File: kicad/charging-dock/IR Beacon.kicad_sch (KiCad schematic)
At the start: 10 parts, among them Q8 IRLML6344TRPBF, U3 TLC555CDR

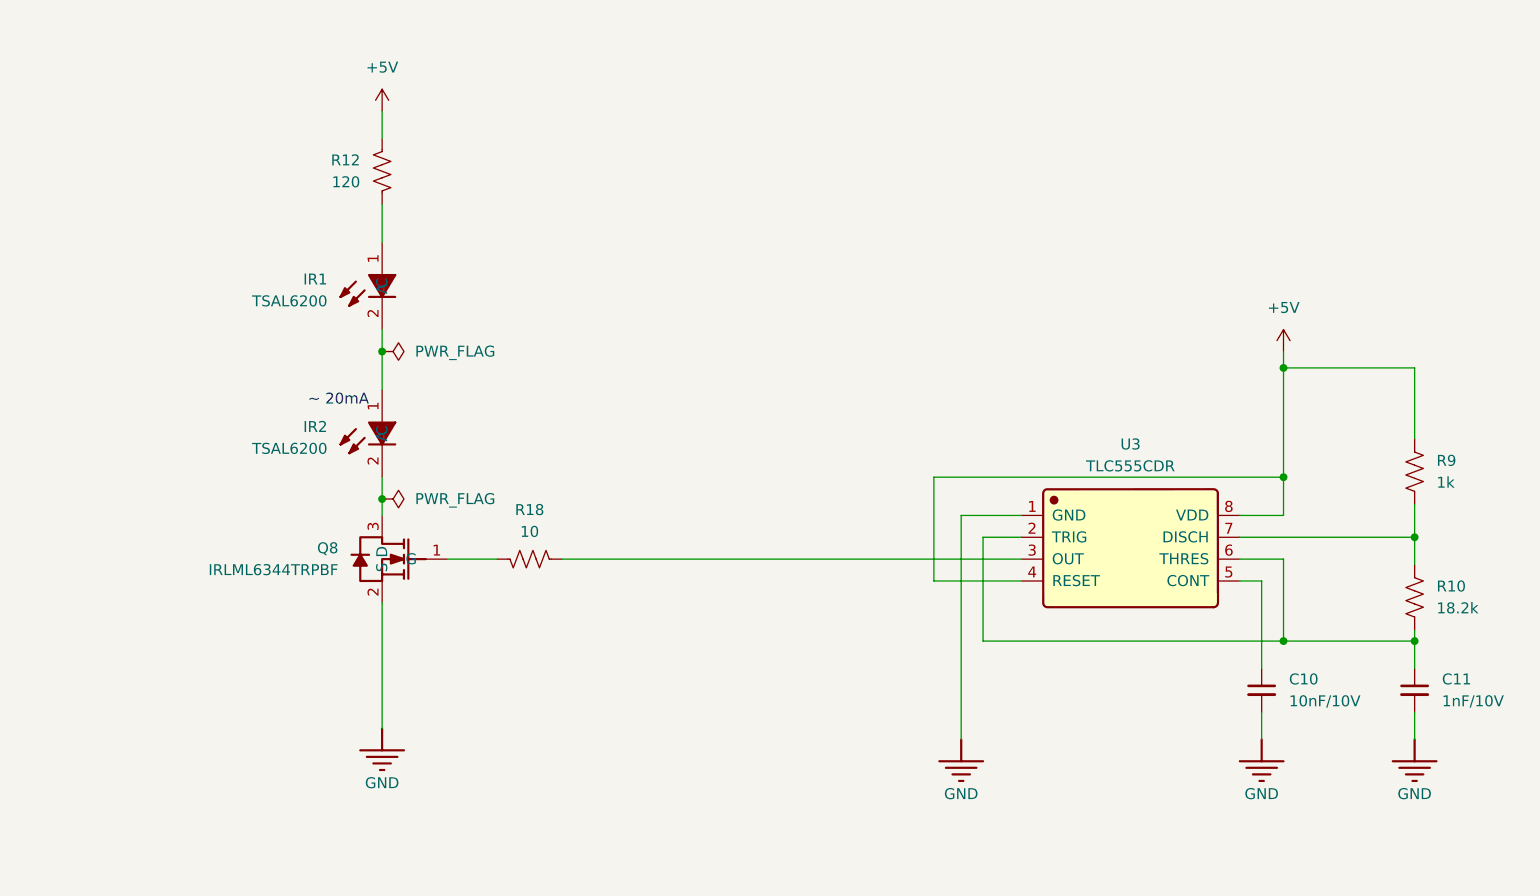
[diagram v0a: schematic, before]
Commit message: Charging dock rev 2; main-phone bucks AP64501 -> TPS54560B
Charging dock (kicad/charging-dock), redesigned:
- CH32V003F4P6 control (Arduino core, ch32fun, PlatformIO)
- robot detection: resistance-signature probe before DOCK+ goes live
- AO4407C soft-start output switch, 50 mOhm + INA180A1 current sense
- NEC IR beacon: two 3x TSAL6200 strings, AC-coupled gates
- 20 V input: DC-044A-20A, 5 A fuse, SMAJ22A, HT7533-1
- refs 8xxx for the one-panel plan; uses the shared ../main libraries
- removed the orphan sheets, the old local library copy and an unrelated PDF
- README with pin map, detection math, firmware rules, layout notes

main-phone: U21/U22 TPS54560B (AP64501 out of stock) with SS56 catch
diodes, 232k RT, 4.7k + 47nF compensation, U21 EN divider; BAT-VCC input
caps 10uF/50V 1206. SPEC and READMEs updated.

Co-Authored-By: Claude Opus 5.5 (1M context) <noreply@anthropic.com>
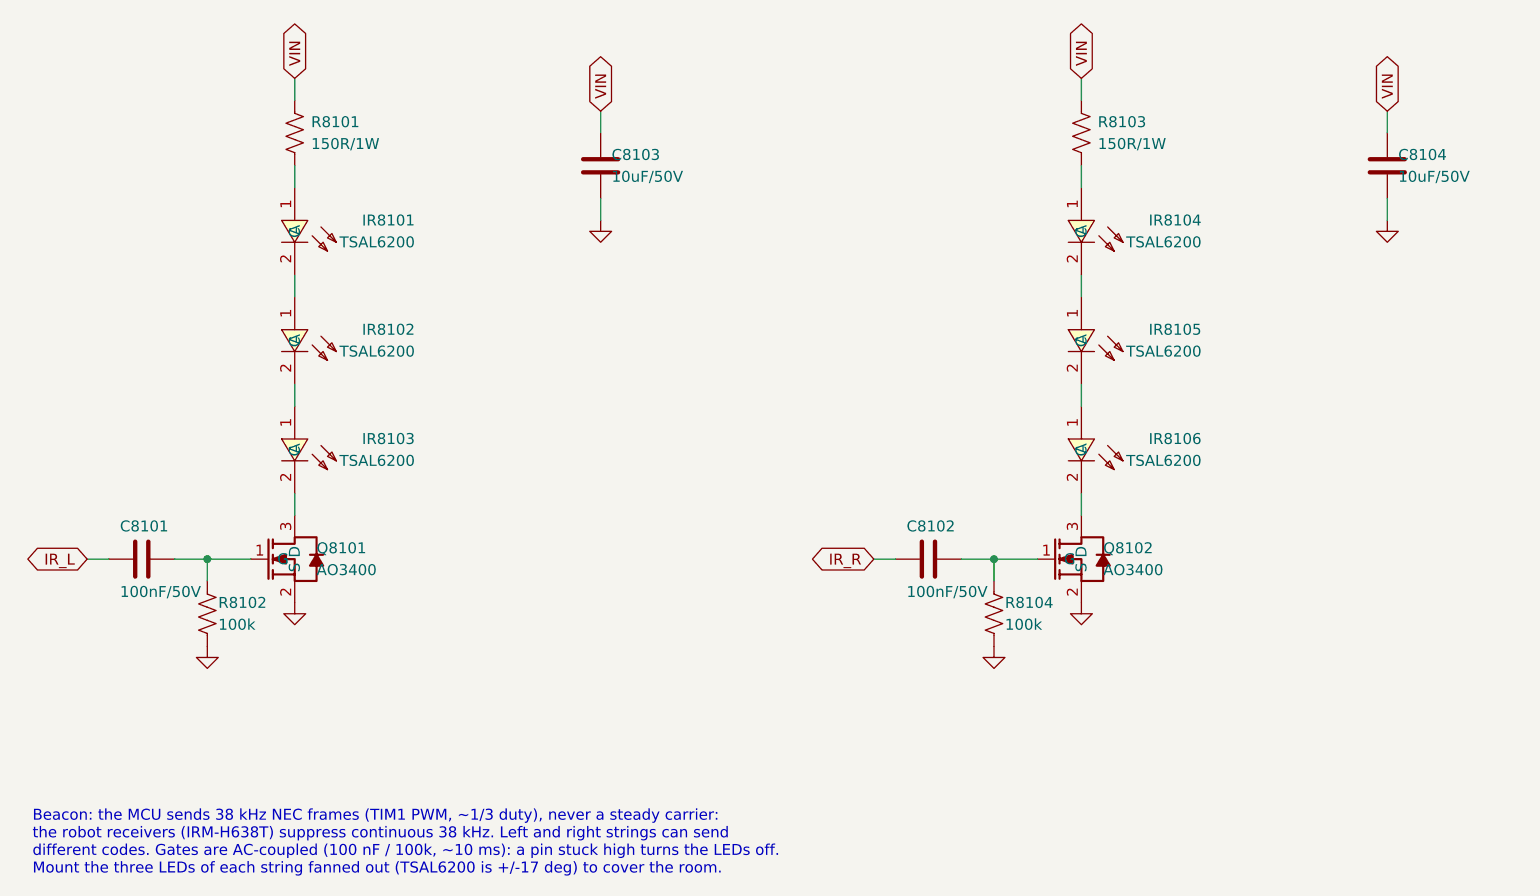
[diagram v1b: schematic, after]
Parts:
- removed C10: 10nF/10V, symbol Device:C_Small
- removed C11: 1nF/10V, symbol Device:C_Small
- removed IR1, IR2: TSAL6200, JLCImport:TSAL6200, symbol JLCImport:TSAL6200
- removed Q8: IRLML6344TRPBF, JLCImport:IRLML6344TRPBF, symbol JLCImport:IRLML6344TRPBF
- removed R10: 18.2k, symbol Device:R_US
- removed R12: 120, symbol Device:R_US
- removed R18: 10, symbol Device:R_US
- removed R9: 1k, symbol Device:R_US
- removed U3: TLC555CDR, JLCImport:TLC555CDR, symbol JLCImport:TLC555CDR
- added C8101, C8102: 100nF/50V, Capacitor_SMD:C_0603_1608Metric, symbol Device:C
- added C8103, C8104: 10uF/50V, Capacitor_SMD:C_1206_3216Metric, symbol Device:C
- added IR8101, IR8102, IR8103, IR8104, IR8105, IR8106: TSAL6200, JLCImport:TSAL6200, symbol JLCImport:TSAL6200
- added Q8101, Q8102: AO3400, JLCImport:AO3400, symbol JLCImport:AO3400
- added R8101, R8103: 150R/1W, Resistor_SMD:R_2512_6332Metric, symbol Device:R_US
- added R8102, R8104: 100k, Resistor_SMD:R_0603_1608Metric, symbol Device:R_US
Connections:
- net GND: now also C8103.2, C8104.2, Q8101.2 (S), Q8102.2 (S), R8102.2, R8104.2
- new net: C8102.2, Q8102.1 (G), R8104.1
- new net: IR8104.1 (A), R8103.2
- new net: IR8104.2 (C), IR8105.1 (A)
- new net: C8101.2, Q8101.1 (G), R8102.1
- new net: IR8101.1 (A), R8101.2
- new net: IR8103.2 (C), Q8101.3 (D)
- new net: IR8101.2 (C), IR8102.1 (A)
- new net: IR8102.2 (C), IR8103.1 (A)
- new net: IR8105.2 (C), IR8106.1 (A)
- new net: IR8106.2 (C), Q8102.3 (D)
- new net IR_L: C8101.1
- new net IR_R: C8102.1
- new net VIN: C8103.1, C8104.1, R8101.1, R8103.1
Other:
- note added: "Beacon: the MCU sends 38 kHz NEC frames (TIM1 PWM, ~1/3 duty), never a steady carrier: the robot receivers (IRM-H638T) suppress continuous 38 kHz. Left and right strings can send different codes. Gates are AC-coupled (100 nF / 100k, ~10 ms): a pin stuck high turns the LEDs off. Mount the three LEDs of each string fanned out (TSAL6200 is +/-17 deg) to cover the room."
- note removed: "~ 20mA"
- company: (none) -> OOMWOO charging dock
- title: (none) -> IR beacon

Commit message: Per-board reference ranges, J1 spare header, IMU AD0 pull-down, BOM outputs
- reference ranges: main-phone 1-999, dock 1000s, front ToF 2000s, side 3000s,
  cliff 4000s, rear IR 5000s, Hall 6000s (main-phone 7xxx parts renumbered
  below 1000; sensor boards and dock moved from 8xxx)
- main-phone: J7301 -> J1, a fitted 2x7 0.1" header with spares only
  (3.3 V, 5 V, I2C4, UART PC10/PC11, PA8-PA10, PD4, PE2, PE6, GND)
- IMU: AP_AD0 pulled low by R217 (address 0x68); INT2 on test pad TP1;
  FSYNC reachable on R211; R18/R72 removed
- tools/export.py replaces export_pdfs.py: schematic PDF and JLC-style BOM in
  each board's output/ folder; --pcb adds Gerbers, placement and STEP
- cliff and rear IR projects: fix top-level sheet left over from a copy
- Hall board: visual tidy-up

Co-Authored-By: Claude Opus 5.5 <noreply@anthropic.com>
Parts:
- renumbered C8101 to C1101, C8102 to C1102, C8103 to C1103, C8104 to C1104, IR8101 to IR1101, IR8102 to IR1102, IR8103 to IR1103, IR8104 to IR1104, IR8105 to IR1105, IR8106 to IR1106, Q8101 to Q1101, Q8102 to Q1102, R8101 to R1101, R8102 to R1102, R8103 to R1103, R8104 to R1104
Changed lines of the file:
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@@
 		(in_pos_files yes)
 		(dnp no)
-		(property "Reference" "R8101"
+		(property "Reference" "R1101"
 			(at 62.865 44.45 0)
 			(show_name no)
@@
 			(project "Charging Dock"
 				(path "/b1780c3e-7100-4df4-97c9-2fd6186fb125/4bb8f12b-f88e-462d-8d8b-7cab36a6773e"
-					(reference "R8101")
+					(reference "R1101")
 					(unit 1)
 				)
@@
 		(in_pos_files yes)
 		(dnp no)
-		(property "Reference" "IR8101"
+		(property "Reference" "IR1101"
 			(at 74.93 55.88 90)
 			(show_name no)
@@
 			(project "Charging Dock"
 				(path "/b1780c3e-7100-4df4-97c9-2fd6186fb125/4bb8f12b-f88e-462d-8d8b-7cab36a6773e"
-					(reference "IR8101")
+					(reference "IR1101")
 					(unit 1)
 				)
@@
 		(in_pos_files yes)
 		(dnp no)
-		(property "Reference" "IR8102"
+		(property "Reference" "IR1102"
 			(at 74.93 68.58 90)
 			(show_name no)
@@
 			(project "Charging Dock"
 				(path "/b1780c3e-7100-4df4-97c9-2fd6186fb125/4bb8f12b-f88e-462d-8d8b-7cab36a6773e"
-					(reference "IR8102")
+					(reference "IR1102")
 					(unit 1)
 				)
@@
 		(in_pos_files yes)
 		(dnp no)
-		(property "Reference" "IR8103"
+		(property "Reference" "IR1103"
 			(at 74.93 81.28 90)
 			(show_name no)
@@
 			(project "Charging Dock"
 				(path "/b1780c3e-7100-4df4-97c9-2fd6186fb125/4bb8f12b-f88e-462d-8d8b-7cab36a6773e"
-					(reference "IR8103")
+					(reference "IR1103")
 					(unit 1)
 				)
@@
 		(in_pos_files yes)
 		(dnp no)
-		(property "Reference" "Q8101"
+		(property "Reference" "Q1101"
 			(at 63.5 93.98 0)
 			(show_name no)
@@
 			(project "Charging Dock"
 				(path "/b1780c3e-7100-4df4-97c9-2fd6186fb125/4bb8f12b-f88e-462d-8d8b-7cab36a6773e"
-					(reference "Q8101")
+					(reference "Q1101")
 					(unit 1)
 				)
@@
 		(in_pos_files yes)
 		(dnp no)
-		(property "Reference" "C8101"
+		(property "Reference" "C1101"
 			(at 40.64 91.44 90)
 			(show_name no)
@@
 			(project "Charging Dock"
 				(path "/b1780c3e-7100-4df4-97c9-2fd6186fb125/4bb8f12b-f88e-462d-8d8b-7cab36a6773e"
-					(reference "C8101")
+					(reference "C1101")
 					(unit 1)
 				)
@@
 		(in_pos_files yes)
 		(dnp no)
-		(property "Reference" "R8102"
+		(property "Reference" "R1102"
 			(at 52.07 100.33 0)
 			(show_name no)
@@
 			(project "Charging Dock"
 				(path "/b1780c3e-7100-4df4-97c9-2fd6186fb125/4bb8f12b-f88e-462d-8d8b-7cab36a6773e"
-					(reference "R8102")
+					(reference "R1102")
 					(unit 1)
 				)
@@
 		(in_pos_files yes)
 		(dnp no)
-		(property "Reference" "R8103"
+		(property "Reference" "R1103"
 			(at 154.305 44.45 0)
 			(show_name no)
@@
 			(project "Charging Dock"
 				(path "/b1780c3e-7100-4df4-97c9-2fd6186fb125/4bb8f12b-f88e-462d-8d8b-7cab36a6773e"
-					(reference "R8103")
+					(reference "R1103")
 					(unit 1)
 				)
@@
 		(in_pos_files yes)
 		(dnp no)
-		(property "Reference" "IR8104"
+		(property "Reference" "IR1104"
 			(at 166.37 55.88 90)
 			(show_name no)
@@
 			(project "Charging Dock"
 				(path "/b1780c3e-7100-4df4-97c9-2fd6186fb125/4bb8f12b-f88e-462d-8d8b-7cab36a6773e"
-					(reference "IR8104")
+					(reference "IR1104")
 					(unit 1)
 				)
@@
 		(in_pos_files yes)
 		(dnp no)
-		(property "Reference" "IR8105"
+		(property "Reference" "IR1105"
 			(at 166.37 68.58 90)
 			(show_name no)
@@
 			(project "Charging Dock"
 				(path "/b1780c3e-7100-4df4-97c9-2fd6186fb125/4bb8f12b-f88e-462d-8d8b-7cab36a6773e"
-					(reference "IR8105")
+					(reference "IR1105")
 					(unit 1)
 				)
@@
 		(in_pos_files yes)
 		(dnp no)
-		(property "Reference" "IR8106"
+		(property "Reference" "IR1106"
 			(at 166.37 81.28 90)
 			(show_name no)
@@
 			(project "Charging Dock"
 				(path "/b1780c3e-7100-4df4-97c9-2fd6186fb125/4bb8f12b-f88e-462d-8d8b-7cab36a6773e"
-					(reference "IR8106")
+					(reference "IR1106")
 					(unit 1)
 				)
@@
 		(in_pos_files yes)
 		(dnp no)
-		(property "Reference" "Q8102"
+		(property "Reference" "Q1102"
 			(at 154.94 93.98 0)
 			(show_name no)
@@
 			(project "Charging Dock"
 				(path "/b1780c3e-7100-4df4-97c9-2fd6186fb125/4bb8f12b-f88e-462d-8d8b-7cab36a6773e"
-					(reference "Q8102")
+					(reference "Q1102")
 					(unit 1)
 				)
@@
 		(in_pos_files yes)
 		(dnp no)
-		(property "Reference" "C8102"
+		(property "Reference" "C1102"
 			(at 132.08 91.44 90)
 			(show_name no)
@@
 			(project "Charging Dock"
 				(path "/b1780c3e-7100-4df4-97c9-2fd6186fb125/4bb8f12b-f88e-462d-8d8b-7cab36a6773e"
-					(reference "C8102")
+					(reference "C1102")
 					(unit 1)
 				)
@@
 		(in_pos_files yes)
 		(dnp no)
-		(property "Reference" "R8104"
+		(property "Reference" "R1104"
 			(at 143.51 100.33 0)
 			(show_name no)
@@
 			(project "Charging Dock"
 				(path "/b1780c3e-7100-4df4-97c9-2fd6186fb125/4bb8f12b-f88e-462d-8d8b-7cab36a6773e"
-					(reference "R8104")
+					(reference "R1104")
 					(unit 1)
 				)
@@
 		(in_pos_files yes)
 		(dnp no)
-		(property "Reference" "C8103"
+		(property "Reference" "C1103"
 			(at 97.79 48.26 0)
 			(show_name no)
@@
 			(project "Charging Dock"
 				(path "/b1780c3e-7100-4df4-97c9-2fd6186fb125/4bb8f12b-f88e-462d-8d8b-7cab36a6773e"
-					(reference "C8103")
+					(reference "C1103")
 					(unit 1)
 				)
@@
 		(in_pos_files yes)
 		(dnp no)
-		(property "Reference" "C8104"
+		(property "Reference" "C1104"
 			(at 189.23 48.26 0)
 			(show_name no)
@@
 			(project "Charging Dock"
 				(path "/b1780c3e-7100-4df4-97c9-2fd6186fb125/4bb8f12b-f88e-462d-8d8b-7cab36a6773e"
-					(reference "C8104")
+					(reference "C1104")
 					(unit 1)
 				)
